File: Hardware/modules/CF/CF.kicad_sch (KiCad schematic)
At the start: 15 parts, among them J1 CF Card, J2 Bus_PCI_6502, U1 74HC00, U2 74LS32, U3 74HCT74, U4 74HC138

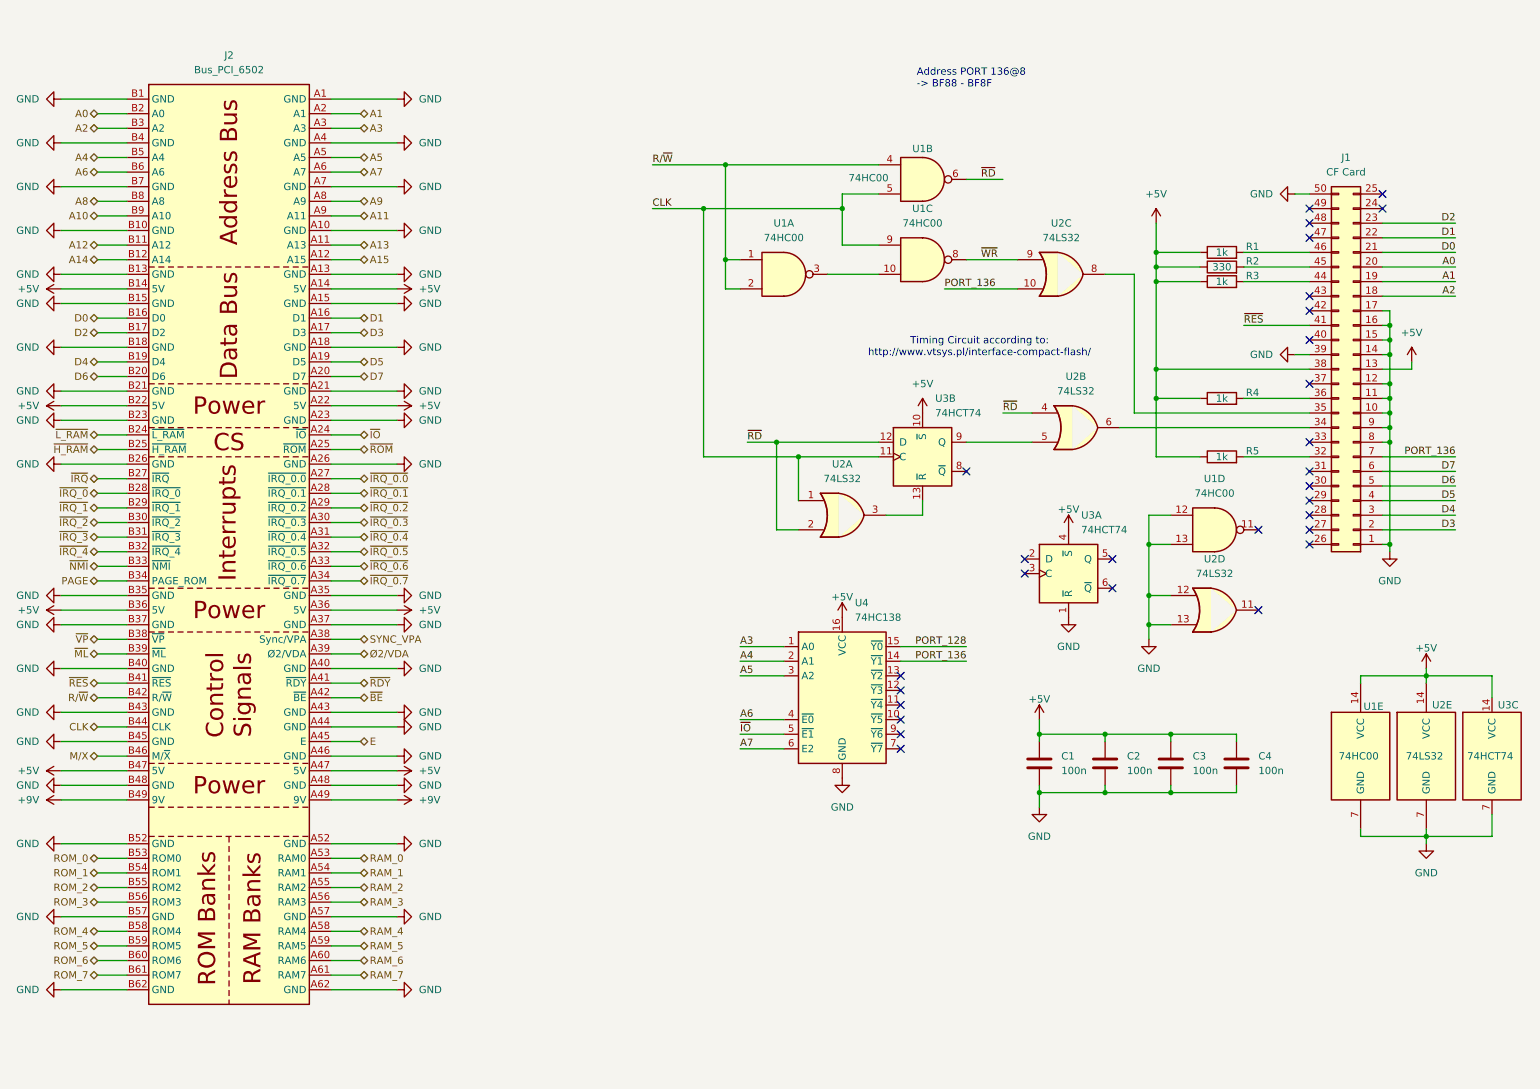
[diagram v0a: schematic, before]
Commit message: Hardware Update Add MyCPU VGA Module Beautify all Schematics minor Error corrections Readme Update
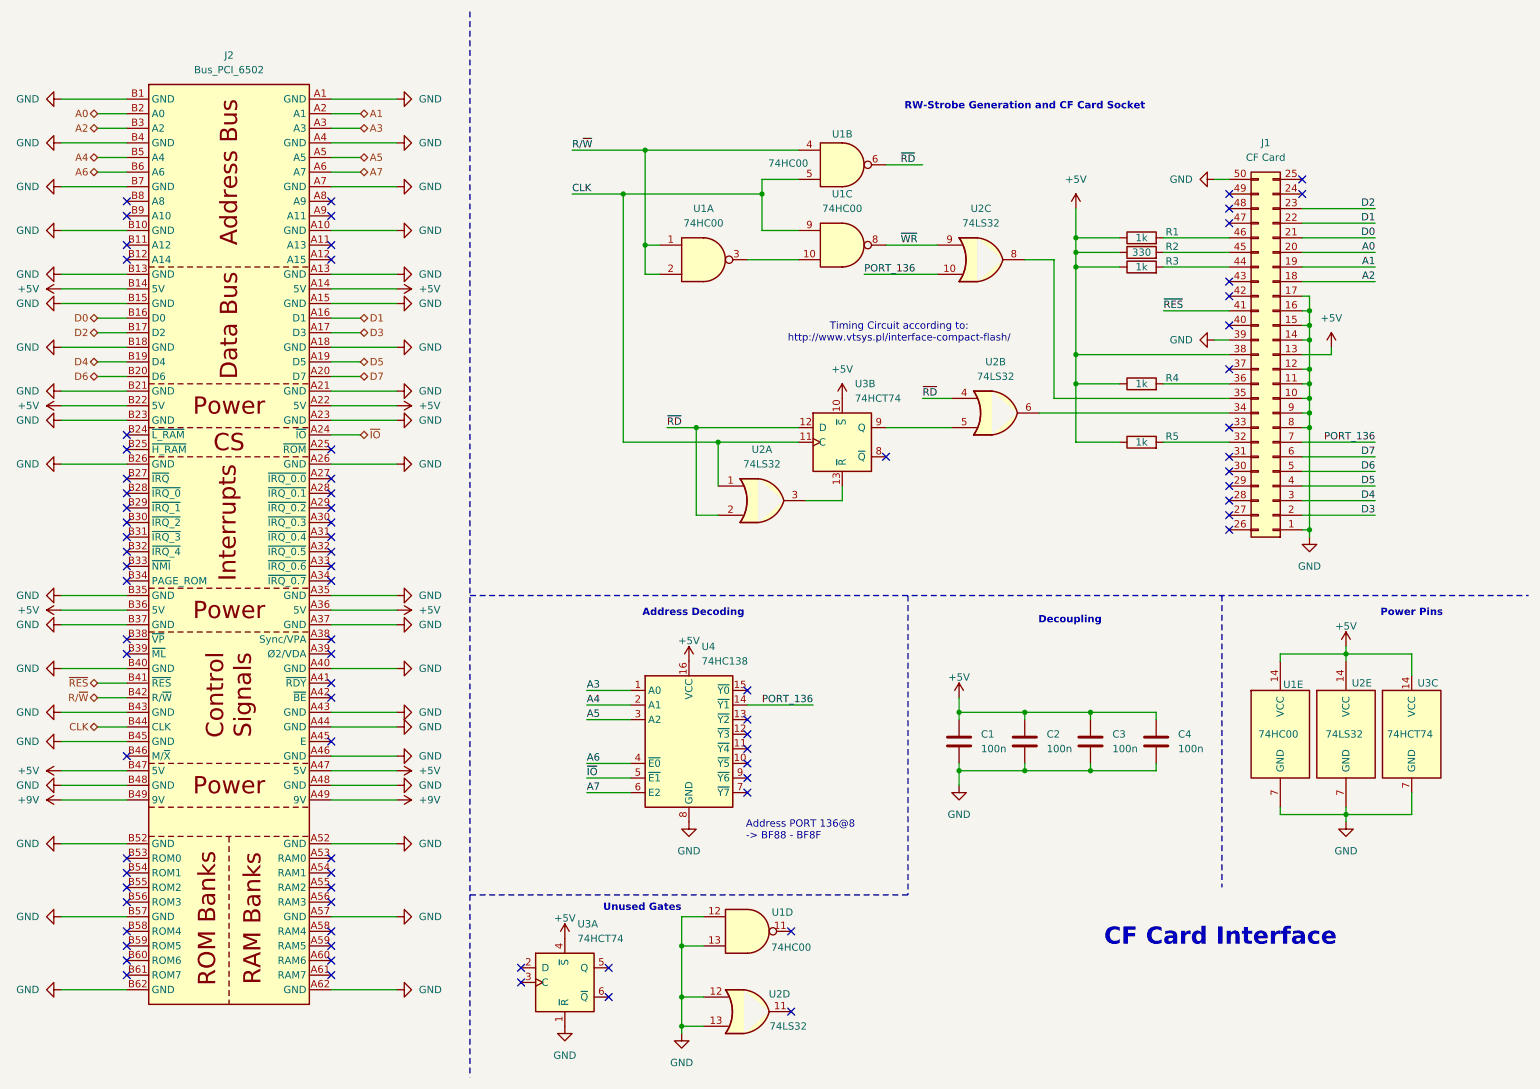
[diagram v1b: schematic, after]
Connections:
- net A10: no longer names the net of J2.B9 (A10)
- net A11: no longer names the net of J2.A9 (A11)
- net A12: no longer names the net of J2.B11 (A12)
- net A13: no longer names the net of J2.A11 (A13)
- net A14: no longer names the net of J2.B12 (A14)
- net A15: no longer names the net of J2.A12 (A15)
- net A8: no longer names the net of J2.B8 (A8)
- net A9: no longer names the net of J2.A8 (A9)
- net E: no longer names the net of J2.A45 (E)
- net M/X: no longer names the net of J2.B46 (M/~{X})
- net PAGE: no longer names the net of J2.B34 (PAGE_ROM)
- net PORT_128: no longer names the net of U4.15 (~{Y0})
- net RAM_0: no longer names the net of J2.A53 (RAM0)
- net RAM_1: no longer names the net of J2.A54 (RAM1)
- net RAM_2: no longer names the net of J2.A55 (RAM2)
- net RAM_3: no longer names the net of J2.A56 (RAM3)
- net RAM_4: no longer names the net of J2.A58 (RAM4)
- net RAM_5: no longer names the net of J2.A59 (RAM5)
- net RAM_6: no longer names the net of J2.A60 (RAM6)
- net RAM_7: no longer names the net of J2.A61 (RAM7)
- net ROM_0: no longer names the net of J2.B53 (ROM0)
- net ROM_1: no longer names the net of J2.B54 (ROM1)
- net ROM_2: no longer names the net of J2.B55 (ROM2)
- net ROM_3: no longer names the net of J2.B56 (ROM3)
- net ROM_4: no longer names the net of J2.B58 (ROM4)
- net ROM_5: no longer names the net of J2.B59 (ROM5)
- net ROM_6: no longer names the net of J2.B60 (ROM6)
- net ROM_7: no longer names the net of J2.B61 (ROM7)
- net SYNC_VPA: no longer names the net of J2.A38 (Sync/VPA)
- net ~{BE}: no longer names the net of J2.A42 (~{BE})
- net ~{H_RAM}: no longer names the net of J2.B25 (~{H_RAM})
- net ~{IRQ_0.0}: no longer names the net of J2.A27 (~{IRQ_0.0})
- net ~{IRQ_0.1}: no longer names the net of J2.A28 (~{IRQ_0.1})
- net ~{IRQ_0.2}: no longer names the net of J2.A29 (~{IRQ_0.2})
- net ~{IRQ_0.3}: no longer names the net of J2.A30 (~{IRQ_0.3})
- net ~{IRQ_0.4}: no longer names the net of J2.A31 (~{IRQ_0.4})
- net ~{IRQ_0.5}: no longer names the net of J2.A32 (~{IRQ_0.5})
- net ~{IRQ_0.6}: no longer names the net of J2.A33 (~{IRQ_0.6})
- net ~{IRQ_0.7}: no longer names the net of J2.A34 (~{IRQ_0.7})
- net ~{IRQ_0}: no longer names the net of J2.B28 (~{IRQ_0})
- net ~{IRQ_1}: no longer names the net of J2.B29 (~{IRQ_1})
- net ~{IRQ_2}: no longer names the net of J2.B30 (~{IRQ_2})
- net ~{IRQ_3}: no longer names the net of J2.B31 (~{IRQ_3})
- net ~{IRQ_4}: no longer names the net of J2.B32 (~{IRQ_4})
- net ~{IRQ}: no longer names the net of J2.B27 (~{IRQ})
- net ~{L_RAM}: no longer names the net of J2.B24 (~{L_RAM})
- net ~{ML}: no longer names the net of J2.B39 (~{ML})
- net ~{NMI}: no longer names the net of J2.B33 (~{NMI})
- net ~{RDY}: no longer names the net of J2.A41 (~{RDY})
- net ~{ROM}: no longer names the net of J2.A25 (~{ROM})
- net ~{VP}: no longer names the net of J2.B38 (~{VP})
- net Ø2/VDA: no longer names the net of J2.A39 (Ø2/VDA)
- no-connect marks 29 -> 81
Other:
- note added: "Address Decoding"
- note added: "CF Card Interface"
- note added: "Decoupling"
- note added: "Power Pins"
- note added: "RW-Strobe Generation and CF Card Socket"
- note added: "Unused Gates"
- company: (none) -> Synthron
- title: (none) -> S65xx Computer System
- moved on the sheet: C1, C2, C3, C4, J1, R1, R2, R3, R4, R5, U1A, U1B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

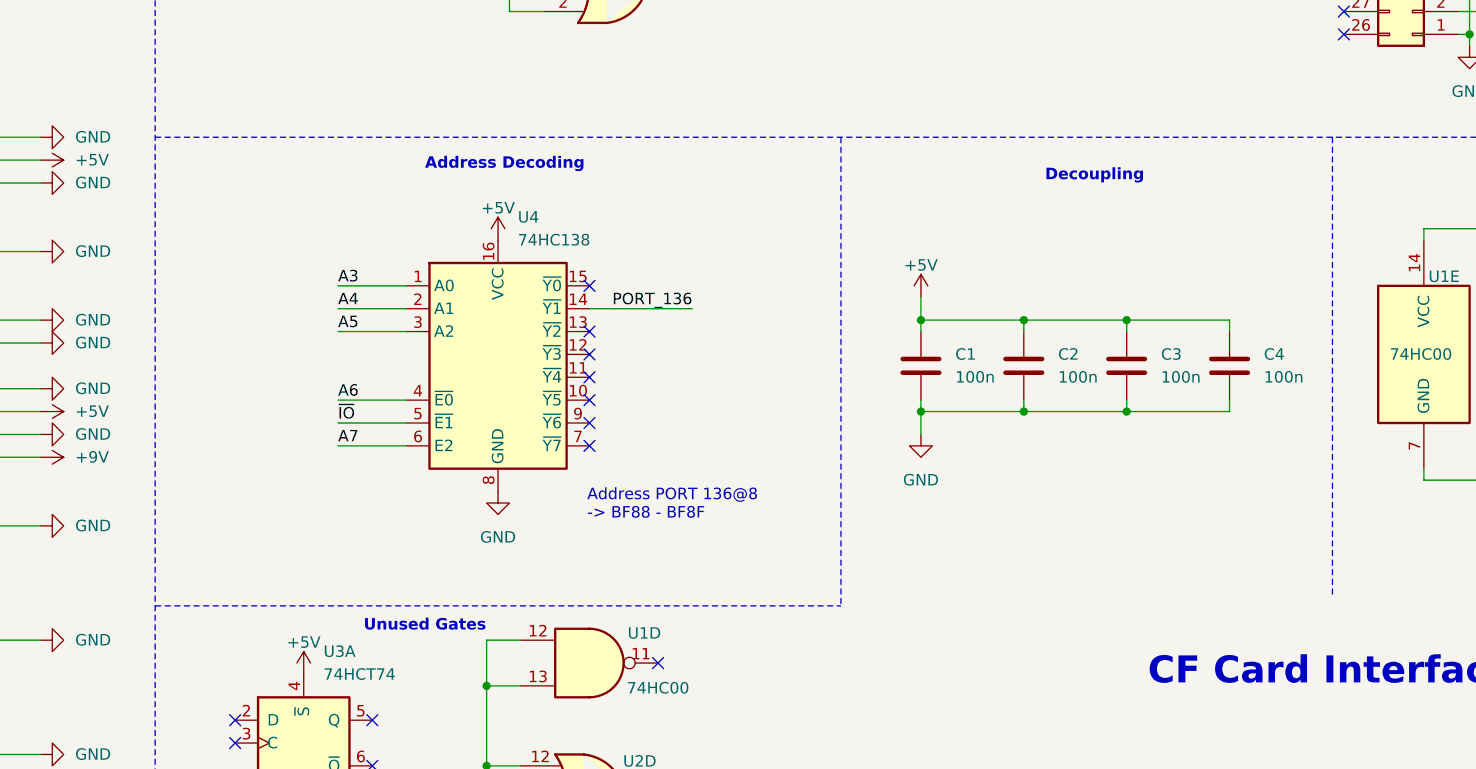
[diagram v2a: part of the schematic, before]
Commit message: Hardware Review Pt. 1 fix Address Decoding for Strobe Generators add bulk capacitance to every board fix wiring of Prototyping Board
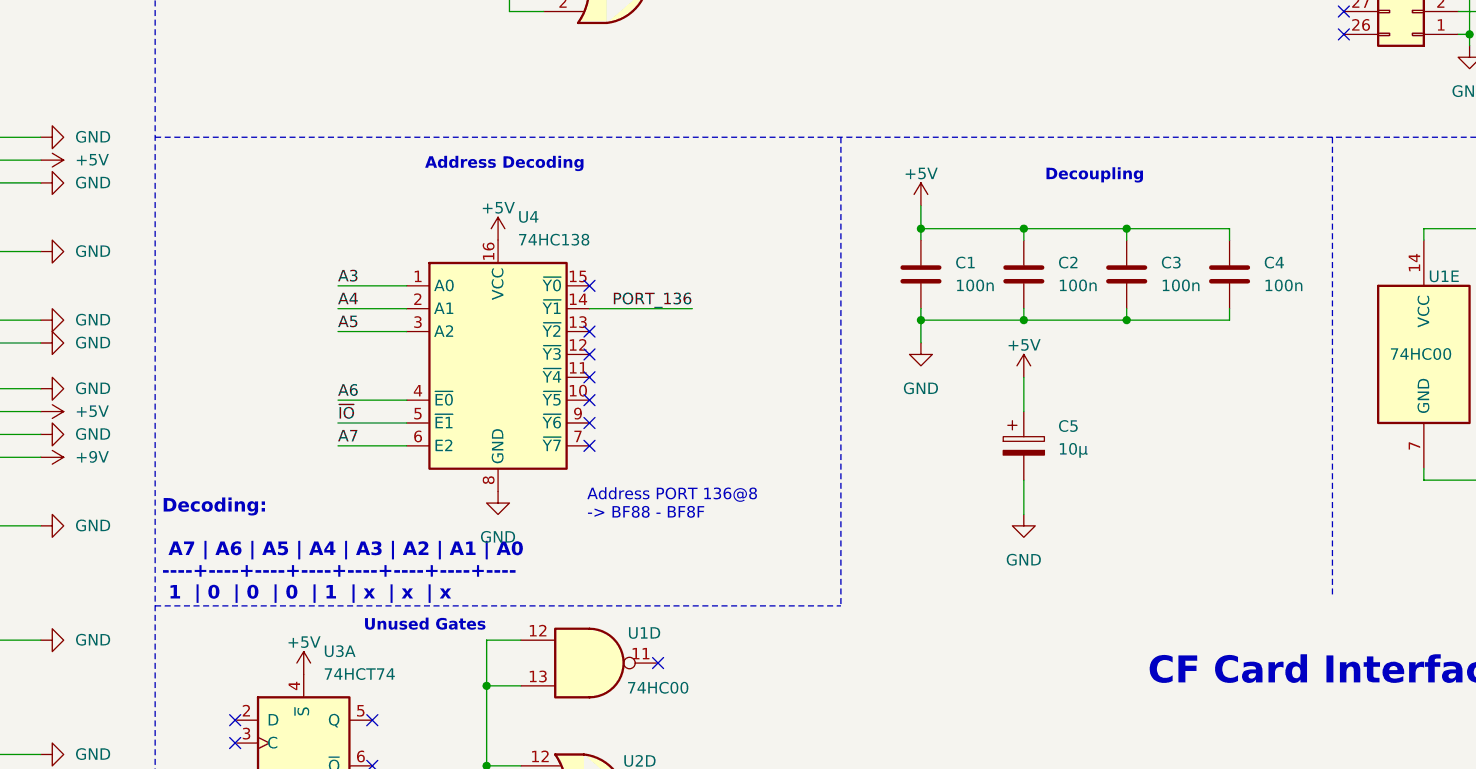
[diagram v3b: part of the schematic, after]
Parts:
- added C5: 10µ, Capacitor_THT:CP_Radial_D5.0mm_P2.50mm, symbol Device:C_Polarized
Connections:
- net +5V: now also C5.1
- net GND: now also C5.2
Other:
- note added: "Decoding: A7 | A6 | A5 | A4 | A3 | A2 | A1 | A0 ----+----+----+----+----+----+----+---- 1 | 0 | 0 | 0 | 1 | x | x | x"
- moved on the sheet: C1, C2, C3, C4
